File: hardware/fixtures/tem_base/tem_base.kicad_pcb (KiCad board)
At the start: 2 copper layers, 140 x 216 mm, 10 parts, among them J1 SMA edge jack (Samtec SMA-J-P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, J2 SMA edge jack (Samtec SMA-J-P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

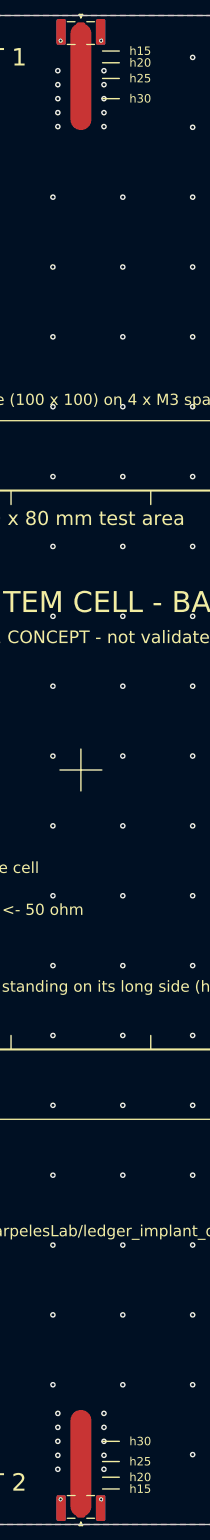
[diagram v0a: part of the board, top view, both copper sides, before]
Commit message: First fixture session: TEM cell sees the implant at every placement
TEM cell (h = 20 mm): the implanted Nano X shows a ~1 dB, ~40 MHz wide
notch at 1171 MHz at every placement and both orientations (sim: -1.2 dB
at 1185 MHz). Six of seven genuine placements stay within 0.2 dB; one
genuine re-check showed a similar notch near 1230 MHz, cause unknown.
Slot line: a small (-0.13..-0.20 dB) dip at 817-861 MHz at 0 deg only.

Also:
- gen_fixtures.py: TEM landing marks now place the ramp tip where the
  rigid ramp's tab actually lands, with the ramp overlapping the septum by
  4 mm; regenerated TEM boards and assembly step 3.
- nanovna_capture.py: zeros mean "outside the active calibration's span"
  (e.g. slot 1 recalled at power-on); say to `recall 0`.

Co-Authored-By: Claude Opus 5.5 <noreply@anthropic.com>
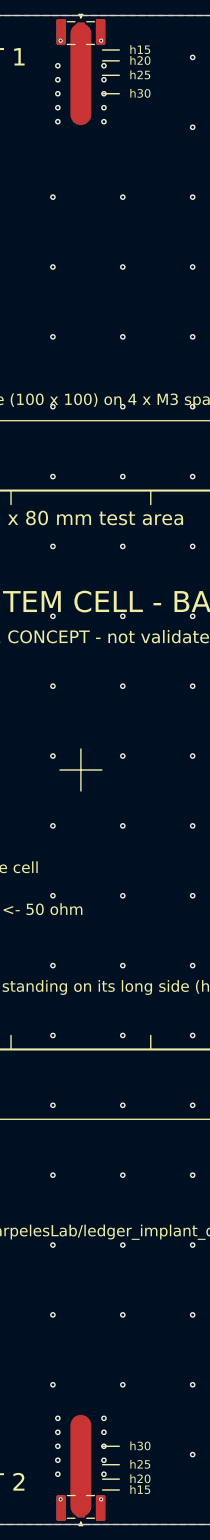
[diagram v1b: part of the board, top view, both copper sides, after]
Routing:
- net P1: track 12.3 -> 11.6 mm
- net P2: track 12.3 -> 11.6 mm
